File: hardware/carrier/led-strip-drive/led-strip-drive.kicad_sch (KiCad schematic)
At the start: 5 parts

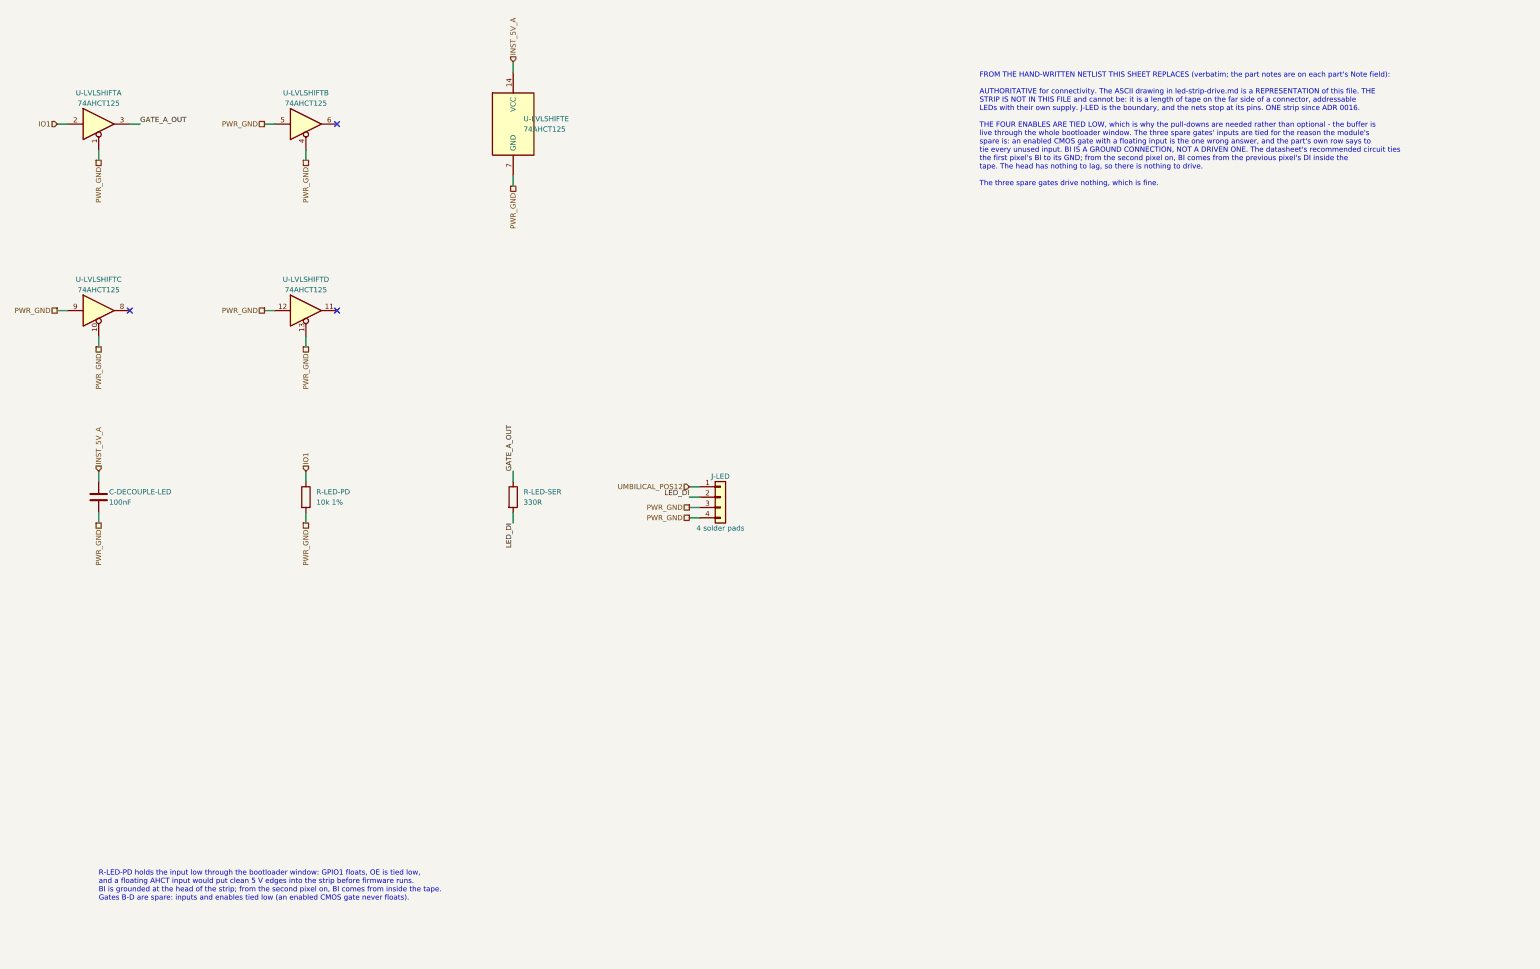
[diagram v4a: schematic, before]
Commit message: LED row: 13 WS2815B-V1 and their 100 nF on the led-strip-drive sheet, J-LED out
The sheet (the source) loses J-LED and gains D-LED-1..13 and C-LED-1..13:
DIN1 from the LED before's DO, DIN2 (the backup input) from the LED
before's DIN1, LED 1's DIN2 to GND, 100 nF VDD to GND at each LED.
Symbol and footprint in hardware/lib (pin 1 NC; the chamfer marks pin 4).
Main board re-exported (D7-D19, C25-C37; ERC 0) and rendered. BOM: D-LED
and C-LED in, J-LED and the LED-STRIP reel out, notes on U-LVLSHIFT,
R-LED-SER, R-LED-PD, C-STRIP-BULK and PCB-CARRIER (white mask). Page
rewritten against the B-V1's V_IH.

Co-Authored-By: Claude Opus 5.5 <noreply@anthropic.com>
Claude-Session: https://claude.ai/code/session_01LmB4muFXnoLprWX4JzuJ5A
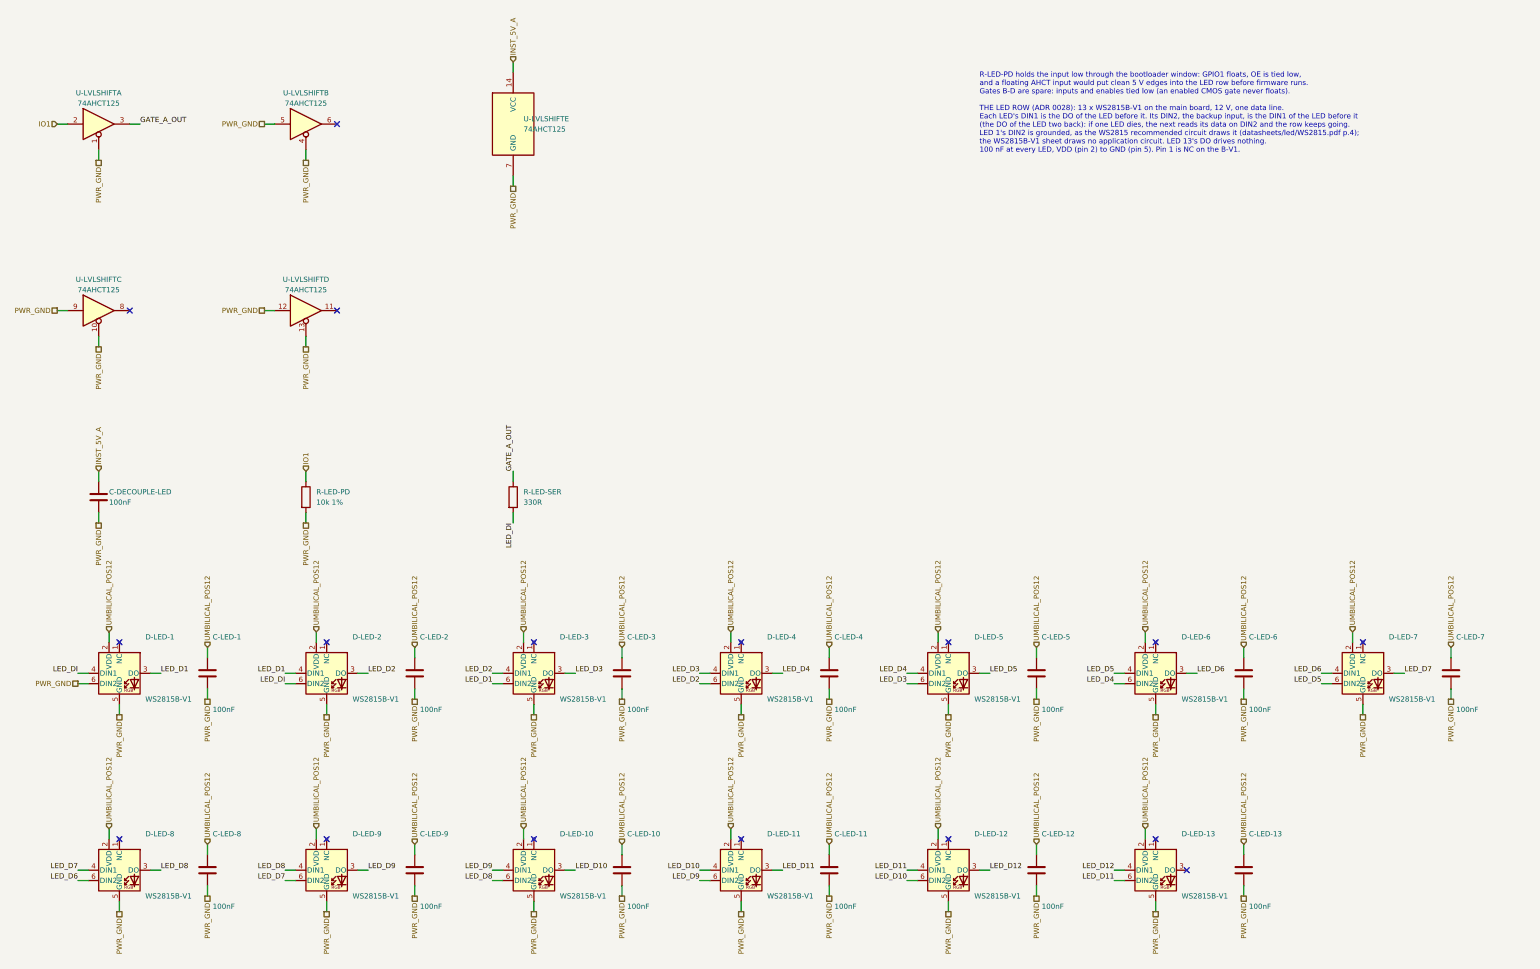
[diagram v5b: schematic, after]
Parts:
- removed J-LED: 4 solder pads, Connector_PinHeader_2.54mm:PinHeader_1x04_P2.54mm_Vertical, symbol Connector_Generic:Conn_01x04
- added C-LED-1, C-LED-10, C-LED-11, C-LED-12, C-LED-13, C-LED-2, C-LED-3, C-LED-4, C-LED-5, C-LED-6, C-LED-7, C-LED-8, C-LED-9: 100nF, Capacitor_SMD:C_0805_2012Metric, symbol Device:C
- added D-LED-1, D-LED-10, D-LED-11, D-LED-12, D-LED-13, D-LED-2, D-LED-3, D-LED-4, D-LED-5, D-LED-6, D-LED-7, D-LED-8, D-LED-9: WS2815B-V1, woody:LED_WS2815B-V1_PLCC6_5.4x5.0mm_P1.6mm, symbol woody:WS2815B-V1
- R-LED-PD: Note PULL-DOWN, and it cannot be added later. GPIO1 is high-impedance for the bootloader window, OE is tied low, and an AHCT input floating near its threshold becomes clean 5 V edges into the strip on a 12 V rail before any firmware runs -> PULL-DOWN, and it cannot be added later. GPIO1 is high-impedance for the bootloader window, OE is tied low, and an AHCT input floating near its threshold becomes clean 5 V edges into the LED row on a 12 V rail before any firmware runs
- R-LED-SER: Note Series into the strip's DI, the vendor's recommended circuit -> Series at the driver into LED 1 DIN1 and LED 2 DIN2 (the ba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
- U-LVLSHIFT: Note ON THE 5 V RAIL, and that is the point: TTL thresholds mean a 3.3 V input reads high, and the output is ~4.4 V minimum into a WS2815 that wants 3.15-3.85 V. Gates B, C and D are spare (ADR 0016: one strip) - the head of the strip grounds its BI rather than being driven -> ON THE 5 V RAIL, and that is the point: TTL thresholds mean a 3.3 V input reads high, and the output (~4.4 V minimum) clears the WS2815B-V1 V_IH (2.7 V min) and stays under its 5.7 V logic-input maximum. Gates B, C and D are spare: the row has one data line, and LED 1 grounds its DIN2 rather than having it driven
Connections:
- net LED_DI: now also D-LED-1.4 (DIN1), D-LED-2.6 (DIN2)
- net PWR_GND: now also C-LED-1.2, C-LED-10.2, C-LED-11.2, C-LED-12.2, C-LED-13.2, C-LED-2.2, C-LED-3.2, C-LED-4.2, C-LED-5.2, C-LED-6.2, C-LED-7.2, C-LED-8.2, C-LED-9.2, D-LED-1.5 (GND), D-LED-1.6 (DIN2), D-LED-10.5 (GND), D-LED-11.5 (GND), D-LED-12.5 (GND), D-LED-13.5 (GND), D-LED-2.5 (GND), D-LED-3.5 (GND), D-LED-4.5 (GND), D-LED-5.5 (GND), D-LED-6.5 (GND), D-LED-7.5 (GND), D-LED-8.5 (GND), D-LED-9.5 (GND)
- net UMBILICAL_POS12: now also C-LED-1.1, C-LED-10.1, C-LED-11.1, C-LED-12.1, C-LED-13.1, C-LED-2.1, C-LED-3.1, C-LED-4.1, C-LED-5.1, C-LED-6.1, C-LED-7.1, C-LED-8.1, C-LED-9.1, D-LED-1.2 (VDD), D-LED-10.2 (VDD), D-LED-11.2 (VDD), D-LED-12.2 (VDD), D-LED-13.2 (VDD), D-LED-2.2 (VDD), D-LED-3.2 (VDD), D-LED-4.2 (VDD), D-LED-5.2 (VDD), D-LED-6.2 (VDD), D-LED-7.2 (VDD), D-LED-8.2 (VDD), D-LED-9.2 (VDD)
- new net LED_D1: D-LED-1.3 (DO), D-LED-2.4 (DIN1), D-LED-3.6 (DIN2)
- new net LED_D10: D-LED-10.3 (DO), D-LED-11.4 (DIN1), D-LED-12.6 (DIN2)
- new net LED_D11: D-LED-11.3 (DO), D-LED-12.4 (DIN1), D-LED-13.6 (DIN2)
- new net LED_D12: D-LED-12.3 (DO), D-LED-13.4 (DIN1)
- new net LED_D2: D-LED-2.3 (DO), D-LED-3.4 (DIN1), D-LED-4.6 (DIN2)
- new net LED_D3: D-LED-3.3 (DO), D-LED-4.4 (DIN1), D-LED-5.6 (DIN2)
- new net LED_D4: D-LED-4.3 (DO), D-LED-5.4 (DIN1), D-LED-6.6 (DIN2)
- new net LED_D5: D-LED-5.3 (DO), D-LED-6.4 (DIN1), D-LED-7.6 (DIN2)
- new net LED_D6: D-LED-6.3 (DO), D-LED-7.4 (DIN1), D-LED-8.6 (DIN2)
- new net LED_D7: D-LED-7.3 (DO), D-LED-8.4 (DIN1), D-LED-9.6 (DIN2)
- new net LED_D8: D-LED-10.6 (DIN2), D-LED-8.3 (DO), D-LED-9.4 (DIN1)
- new net LED_D9: D-LED-10.4 (DIN1), D-LED-11.6 (DIN2), D-LED-9.3 (DO)
- no-connect marks 3 -> 17
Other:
- note added: "R-LED-PD holds the input low through the bootloader window: GPIO1 floats, OE is tied low, and a floating AHCT input would put clean 5 V edges into the LED row before firmware runs. Gates B-D are spare: inputs and enables tied low (an enabled CMOS gate never floats). THE LED ROW (ADR 0028): 13 x WS2815B-V1 on the main board, 12 V, one data line. Each LED's DIN1 is the DO of the LED before it. Its 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"
- note removed: "FROM THE HAND-WRITTEN NETLIST THIS SHEET REPLACES (verbatim; the part notes are on each part's Note field): AUTHORITATIVE for connectivity. The ASCII drawing in led-strip-drive.md is a REPRESENTATION of this file. THE STRIP IS NOT IN THIS FILE and cannot be: it is a length of tape on the far side of a connector, addressable LEDs with their own supply. J-LED is the boundary, and the nets stop at i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"
- note removed: "R-LED-PD holds the input low through the bootloader window: GPIO1 floats, OE is tied low, and a floating AHCT input would put clean 5 V edges into the strip before firmware runs. BI is grounded at the head of the strip; from the second pixel on, BI comes from inside the tape. Gates B-D are spare: inputs and enables tied low (an enabled CMOS gate never floats)."
- title: LED strip drive (hardware/carrier/led-strip-drive) -> LED drive and the LED row (hardware/carrier/led-strip-drive)

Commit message: Instrument power entry: Q-INRUSH soft start between the connector and the bulk (sheets, WIP)
Q-INRUSH (AO3401A) and its gate network on the power-entry-instrument sheet;
the switched side is INST_POS12, which the LED drive and the analog reference
now receive. Exported; main board ERC clean. BOM, nets, sims and pages follow.

Co-Authored-By: Claude Opus 5.5 <noreply@anthropic.com>
Claude-Session: https://claude.ai/code/session_01LmB4muFXnoLprWX4JzuJ5A
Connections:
- net UMBILICAL_POS12 renamed INST_POS12

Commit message: LED drive: D-LED-14 and C-LED-14 on the sheet; the corner LED is D-LED-1, the chain unchanged
The sheet gains a fourteenth LED and its 100 nF at the chain's end; on the
main board the references run in chain order (D7..D20, C25..C38), so
D-INRUSH-RST is D21 and C-INRUSH-GS/GD C39/C40 (layout.yaml keys follow).
BOM fragment qty 14; netlist and board-netlist re-exported.

Co-Authored-By: Claude Opus 5.5 <noreply@anthropic.com>
Claude-Session: https://claude.ai/code/session_01LmB4muFXnoLprWX4JzuJ5A
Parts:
- added C-LED-14: 100nF, Capacitor_SMD:C_0805_2012Metric, symbol Device:C
- added D-LED-14: WS2815B-V1, woody:LED_WS2815B-V1_PLCC6_5.4x5.0mm_P1.6mm, symbol woody:WS2815B-V1
- D-LED-1, D-LED-10, D-LED-11, D-LED-12, D-LED-13, D-LED-2, D-LED-3, D-LED-4, D-LED-5, D-LED-6, D-LED-7, D-LED-8, D-LED-9: Note On the main board's top face, one row on the centreline (AD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 -> On the main board's top face (ADR 0028): D-LED-1 in the tai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
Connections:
- net INST_POS12: now also C-LED-14.1, D-LED-14.2 (VDD)
- net LED_D12: now also D-LED-14.6 (DIN2)
- net PWR_GND: now also C-LED-14.2, D-LED-14.5 (GND)
- net LED_D13: now reaches D-LED-13.3 (DO)
- net LED_D13: now also D-LED-14.4 (DIN1)
- no-connect marks 17 -> 18
